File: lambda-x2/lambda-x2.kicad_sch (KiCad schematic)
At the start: 126 parts, among them J1 FTSH-107-01-F-DV-K, J3 Conn_02x02_Odd_Even, J4 Conn_01x10, P1 33311-24AW-2, Q1 BTS3028, Q2 BTS3028, Q3 BTS3028, Q4 BTS3028, U17 MCP6002T-I/SN, U18 JDY-33, U2 STM32F103C6Tx, U4 LM78M05_TO252, U5 XC6206P332MR, U6 REF3033, U7 MCP6002T-I/SN, U8 TJA1051T-3

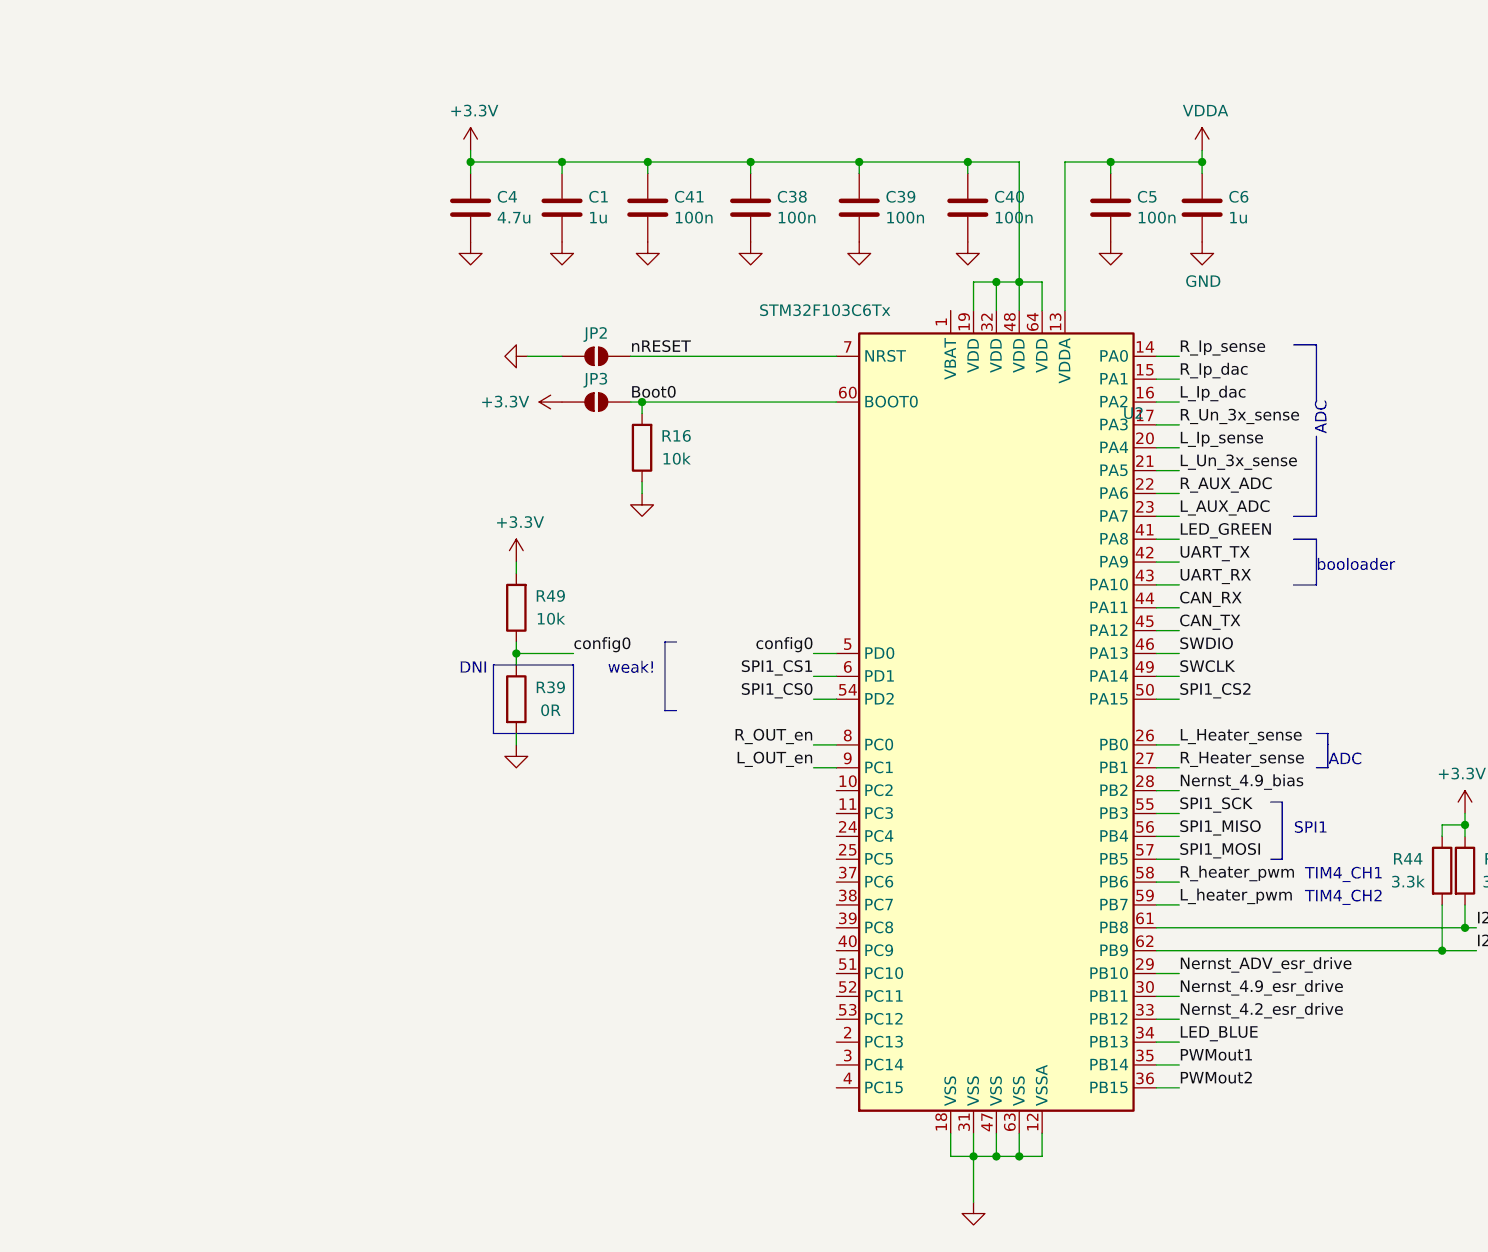
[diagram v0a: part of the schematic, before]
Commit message: lambda-x2: add HSE, move pump to DAC outputs
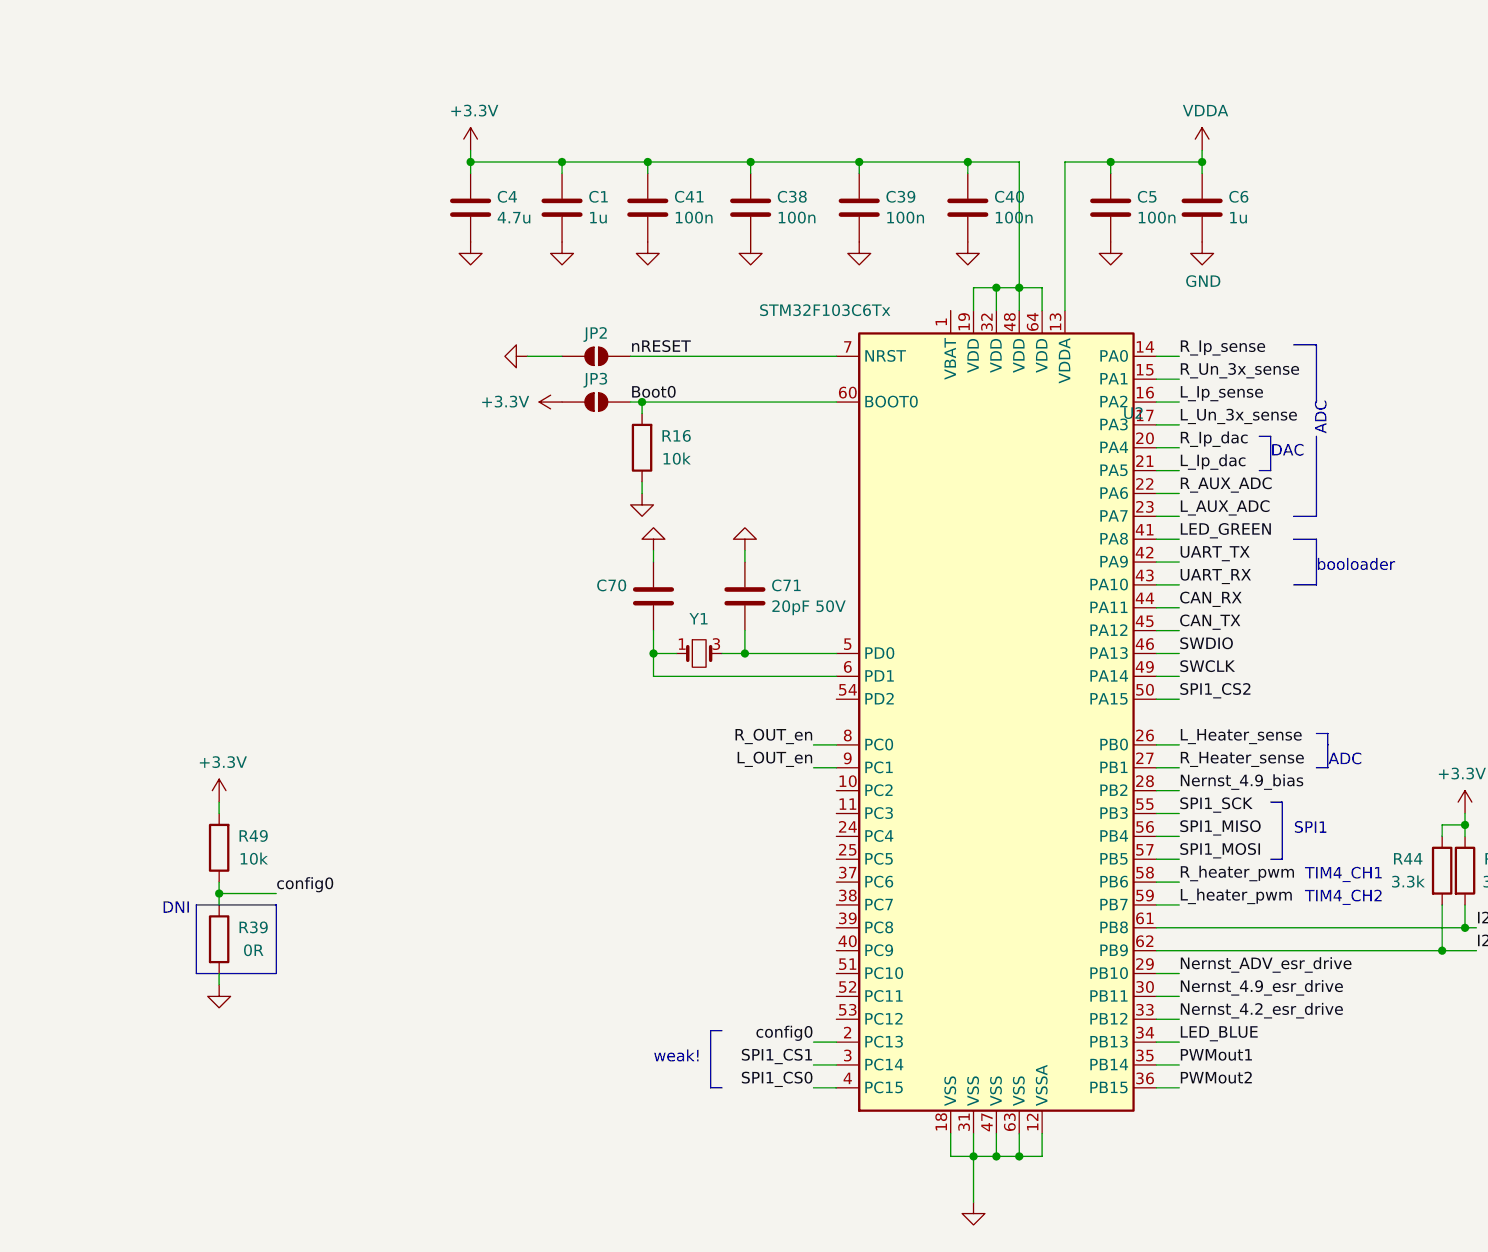
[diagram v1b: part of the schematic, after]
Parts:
- added C70: (no value), symbol Device:C
- added C71: 20pF 50V, Capacitor_SMD:C_0402_1005Metric, symbol Device:C
- added Y1: (no value), symbol Device:Crystal_Small
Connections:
- net GND: now also C70.1, C71.1
- net L_Ip_dac: now also U2.21 (PA5); no longer U2.16 (PA2)
- net L_Ip_sense: now also U2.16 (PA2); no longer U2.20 (PA4)
- net L_Un_3x_sense: now also U2.17 (PA3); no longer U2.21 (PA5)
- net R_Ip_dac: now also U2.20 (PA4); no longer U2.15 (PA1)
- net R_Un_3x_sense: now also U2.15 (PA1); no longer U2.17 (PA3)
- net SPI1_CS0: now also U2.4 (PC15); no longer U2.54 (PD2)
- net SPI1_CS1: now also U2.3 (PC14); no longer U2.6 (PD1)
- net config0: now also U2.2 (PC13); no longer U2.5 (PD0)
- new net: C70.2, U2.6 (PD1), Y1.1
- new net: C71.2, U2.5 (PD0), Y1.3
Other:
- note added: "DAC"
- moved on the sheet: R39, R49

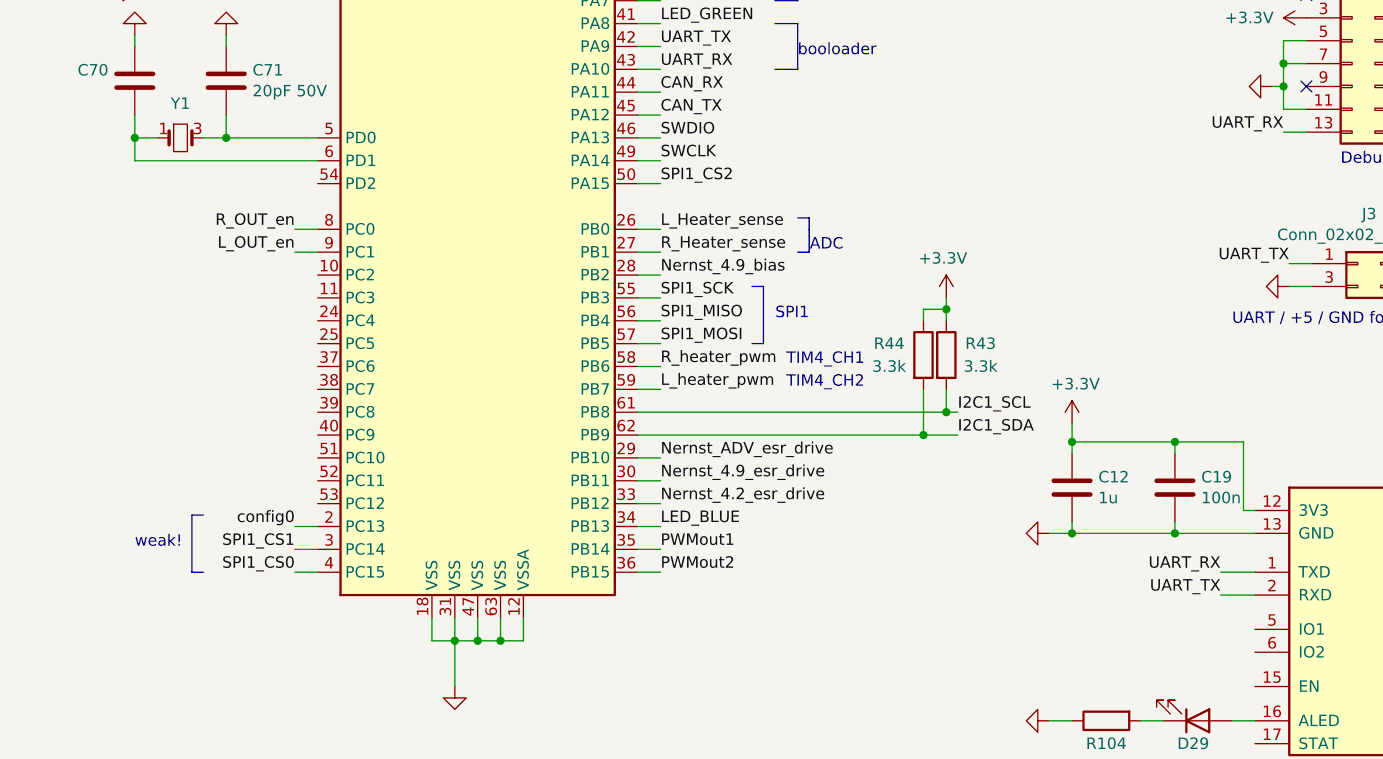
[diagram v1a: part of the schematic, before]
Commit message: lambda-x2: move BT to UART4/USART3
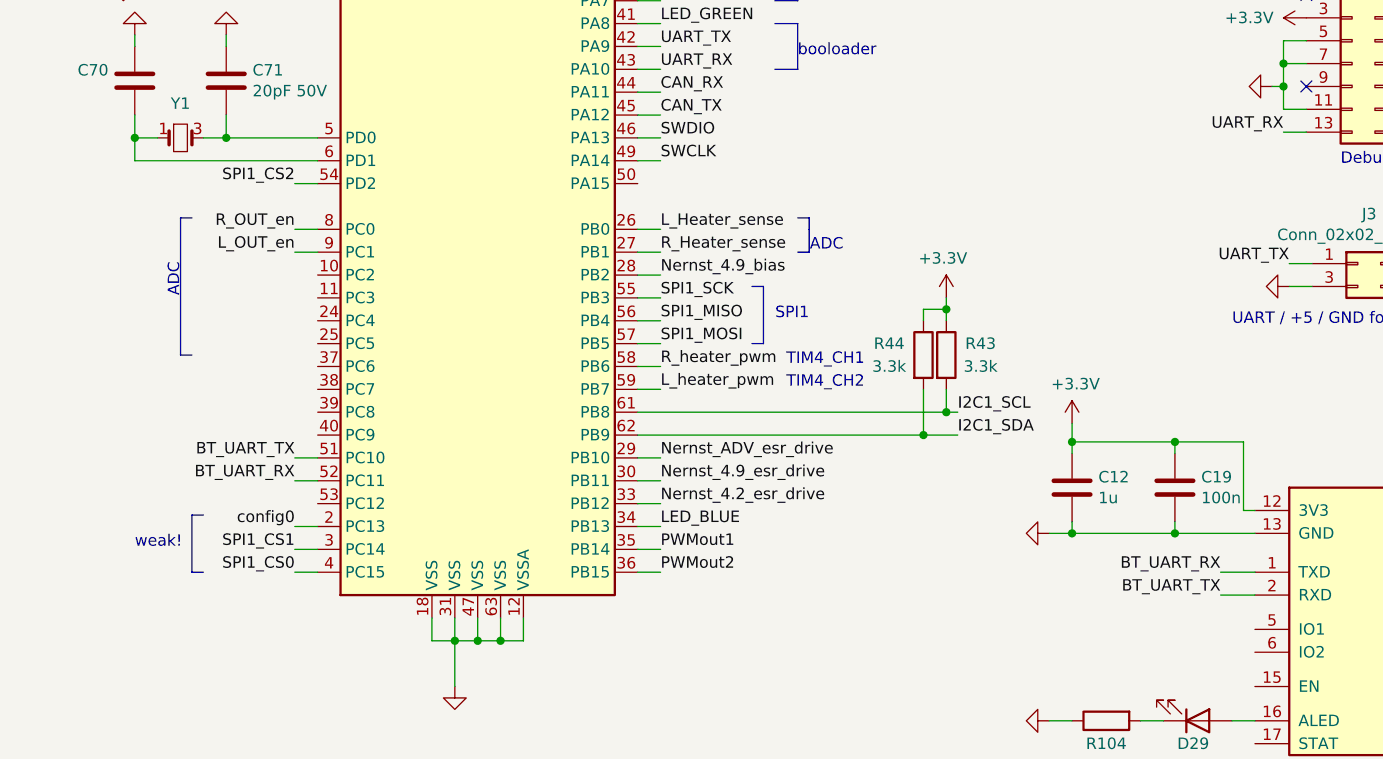
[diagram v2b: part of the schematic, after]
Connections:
- net SPI1_CS2: now also U2.54 (PD2); no longer U2.50 (PA15)
- net UART_RX: no longer U18.1 (TXD)
- net UART_TX: no longer U18.2 (RXD)
- net BT_UART_TX: now reaches U2.51 (PC10)
- net BT_UART_TX: now also U18.2 (RXD)
- net BT_UART_RX: now reaches U2.52 (PC11)
- net BT_UART_RX: now also U18.1 (TXD)
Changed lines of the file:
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@@
+    (stroke (width 0) (type default) (color 0 0 0 0))
+  )
+  (wire (pts (xy 370.84 203.2) (xy 373.38 203.2))
     (stroke (width 0) (type default) (color 0 0 0 0))
   )
@@
     (stroke (width 0) (type default) (color 0 0 0 0))
   )
+  (polyline (pts (xy 359.41 176.53) (xy 358.14 176.53))
+    (stroke (width 0) (type default) (color 0 0 0 0))
+  )
   (polyline (pts (xy 359.41 45.72) (xy 367.03 45.72))
     (stroke (width 0) (type default) (color 0 0 0 0))
@@
     (stroke (width 0) (type default) (color 0 0 0 0))
   )
+  (wire (pts (xy 370.84 172.72) (xy 373.38 172.72))
+    (stroke (width 0) (type default) (color 0 0 0 0))
+  )
   (wire (pts (xy 480.695 161.925) (xy 480.695 159.385))
     (stroke (width 0) (type default) (color 0 0 0 0))
@@
     (stroke (width 0) (type default) (color 0 0 0 0))
   )
+  (polyline (pts (xy 358.14 176.53) (xy 358.14 191.77))
+    (stroke (width 0) (type default) (color 0 0 0 0))
+  )
   (wire (pts (xy 499.11 181.61) (xy 496.57 181.61))
     (stroke (width 0) (type default) (color 0 0 0 0))
@@
     (stroke (width 0) (type default) (color 0 0 0 0))
   )
+  (wire (pts (xy 370.84 205.74) (xy 373.38 205.74))
+    (stroke (width 0) (type default) (color 0 0 0 0))
+  )
   (wire (pts (xy 340.36 34.29) (xy 342.9 34.29))
     (stroke (width 0) (type default) (color 0 0 0 0))
@@
     (stroke (width 0) (type default) (color 0 0 0 0))
   )
+  (polyline (pts (xy 358.14 191.77) (xy 359.41 191.77))
+    (stroke (width 0) (type default) (color 0 0 0 0))
+  )
   (polyline (pts (xy 311.15 203.2) (xy 302.26 203.2))
     (stroke (width 0) (type default) (color 0 0 0 0))
@@
     (stroke (width 0) (type default) (color 0 0 0 0))
   )
-  (wire (pts (xy 408.94 172.72) (xy 411.48 172.72))
-    (stroke (width 0) (type default) (color 0 0 0 0))
-  )
   (wire (pts (xy 190.5 331.47) (xy 191.77 331.47))
     (stroke (width 0) (type default) (color 0 0 0 0))
@@
     (effects (font (size 1.27 1.27)) (justify right bottom))
   )
+  (text "ADC" (at 358.14 181.61 270)
+    (effects (font (size 1.27 1.27)) (justify right bottom))
+  )
   (text "red" (at 80.01 88.9 0)
     (effects (font (size 1.27 1.27)) (justify left bottom))
@@
     (effects (font (size 1.27 1.27)) (justify left bottom))
   )
-  (label "UART_RX" (at 473.71 215.9 180)
-    (effects (font (size 1.27 1.27)) (justify right bottom))
-  )
   (label "R_heater_pwm" (at 234.95 234.95 0)
     (effects (font (size 1.27 1.27)) (justify left bottom))
@@
     (effects (font (size 1.27 1.27)) (justify left bottom))
   )
+  (label "BT_UART_RX" (at 370.84 205.74 180)
+    (effects (font (size 1.27 1.27)) (justify right bottom))
+  )
   (label "R_LSU_Vm" (at 156.21 114.3 180)
     (effects (font (size 1.27 1.27)) (justify right bottom))
@@
     (effects (font (size 1.27 1.27)) (justify left bottom))
   )
-  (label "UART_TX" (at 473.71 218.44 180)
-    (effects (font (size 1.27 1.27)) (justify right bottom))
-  )
   (label "SPI1_CS0" (at 234.95 151.13 0)
     (effects (font (size 1.27 1.27)) (justify left bottom))
   )
-  (label "SPI1_CS2" (at 411.48 172.72 0)
-    (effects (font (size 1.27 1.27)) (justify left bottom))
+  (label "SPI1_CS2" (at 370.84 172.72 180)
+    (effects (font (size 1.27 1.27)) (justify right bottom))
   )
   (label "CAN_H" (at 127 383.54 180)
@@
     (effects (font (size 1.27 1.27)) (justify right bottom))
   )
+  (label "BT_UART_TX" (at 370.84 203.2 180)
+    (effects (font (size 1.27 1.27)) (justify right bottom))
+  )
   (label "Nernst_4.9_esr_drive" (at 208.28 106.68 0)
     (effects (font (size 1.27 1.27)) (justify left bottom))
@@
     (effects (font (size 1.27 1.27)) (justify left bottom))
   )
+  (label "BT_UART_TX" (at 473.71 218.44 180)
+    (effects (font (size 1.27 1.27)) (justify right bottom))
+  )
   (label "R_OD" (at 64.77 121.92 0)
     (effects (font (size 1.27 1.27)) (justify left bottom))
@@
     (effects (font (size 1.27 1.27)) (justify right bottom))
   )
+  (label "BT_UART_RX" (at 473.71 215.9 180)
+    (effects (font (size 1.27 1.27)) (justify right bottom))
+  )

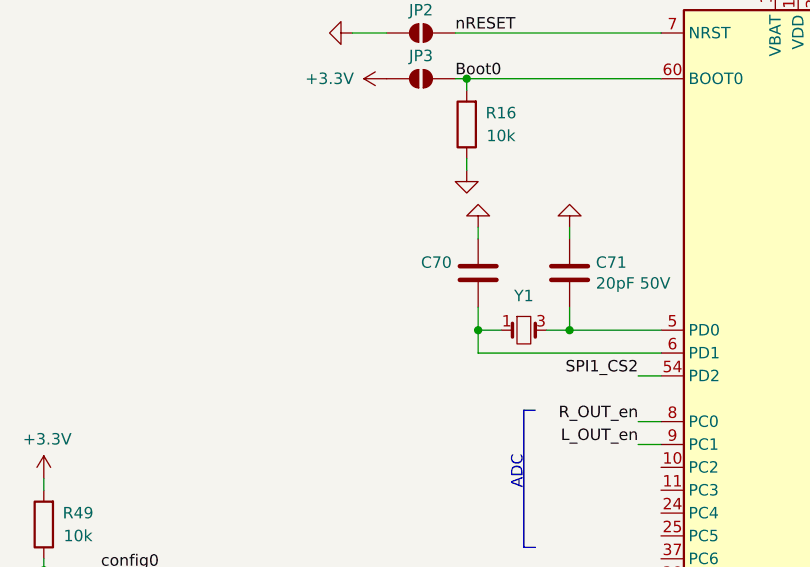
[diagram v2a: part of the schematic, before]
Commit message: lambda-x2: ocsillator fix
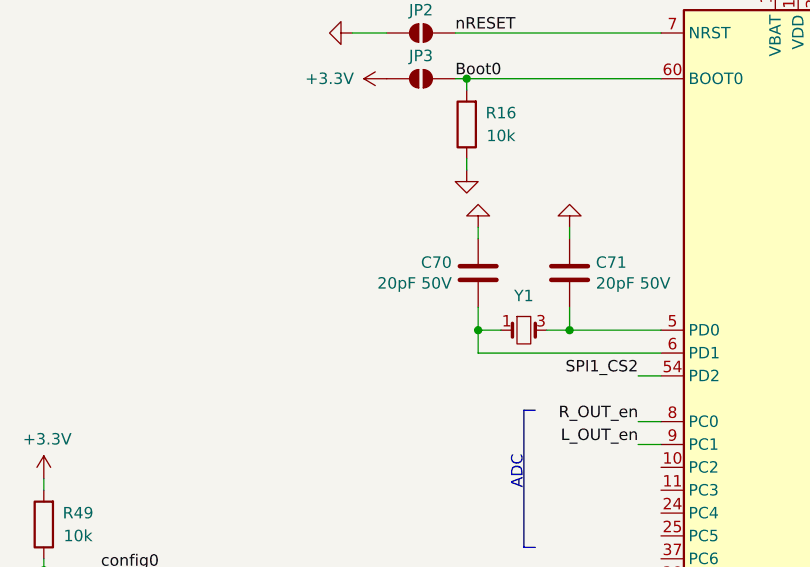
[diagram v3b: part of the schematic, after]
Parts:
- C70: value (none) -> 20pF 50V; footprint (none) -> Capacitor_SMD:C_0402_1005Metric
- Y1: value (none) -> XXDCELNANF-8MHZ; footprint (none) -> Crystal:Crystal_SMD_3225-4Pin_3.2x2.5mm
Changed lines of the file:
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@@
     (in_bom yes) (on_board yes)
     (property "Reference" "Y1" (id 0) (at 358.14 163.83 0))
-    (property "Value" "" (id 1) (at 358.14 171.45 0)
-      (effects (font (size 1.27 1.27)) hide)
-    )
-    (property "Footprint" "" (id 2) (at 358.14 167.64 0)
+    (property "Value" "XXDCELNANF-8MHZ" (id 1) (at 358.14 171.45 0)
+      (effects (font (size 1.27 1.27)) hide)
+    )
+    (property "Footprint" "Crystal:Crystal_SMD_3225-4Pin_3.2x2.5mm" (id 2) (at 358.14 167.64 0)
       (effects (font (size 1.27 1.27)) hide)
     )
@@
       (effects (font (size 1.27 1.27)) (justify left))
     )
-    (property "Value" "" (id 1) (at 350.139 162.433 0)
-      (effects (font (size 1.27 1.27)) (justify left))
-    )
-    (property "Footprint" "" (id 2) (at 352.0948 165.1 0)
-      (effects (font (size 1.27 1.27)) hide)
-    )
+    (property "Value" "20pF 50V" (id 1) (at 350.139 162.433 0)
+      (effects (font (size 1.27 1.27)) (justify left))
+    )
+    (property "Footprint" "Capacitor_SMD:C_0402_1005Metric" (id 2) (at 352.0948 165.1 0)
+      (effects (font (size 1.27 1.27)) hide)
+    )
